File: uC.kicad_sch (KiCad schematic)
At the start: 11 parts, among them P12 Conn_02x10_Odd_Even, SW1 SW_MEC_5E, U2(J1) RPi-Pico

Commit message: Avances en corrección de errores en conexiones eléctricas (ERC).
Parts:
- gave numbers to parts that had none: 1
- renumbered C2 to C1, C1 to C2, D1 to D17, R19 to R1, R19 to R2, U2(J1) to U1
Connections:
- no-connect marks 8 -> 14

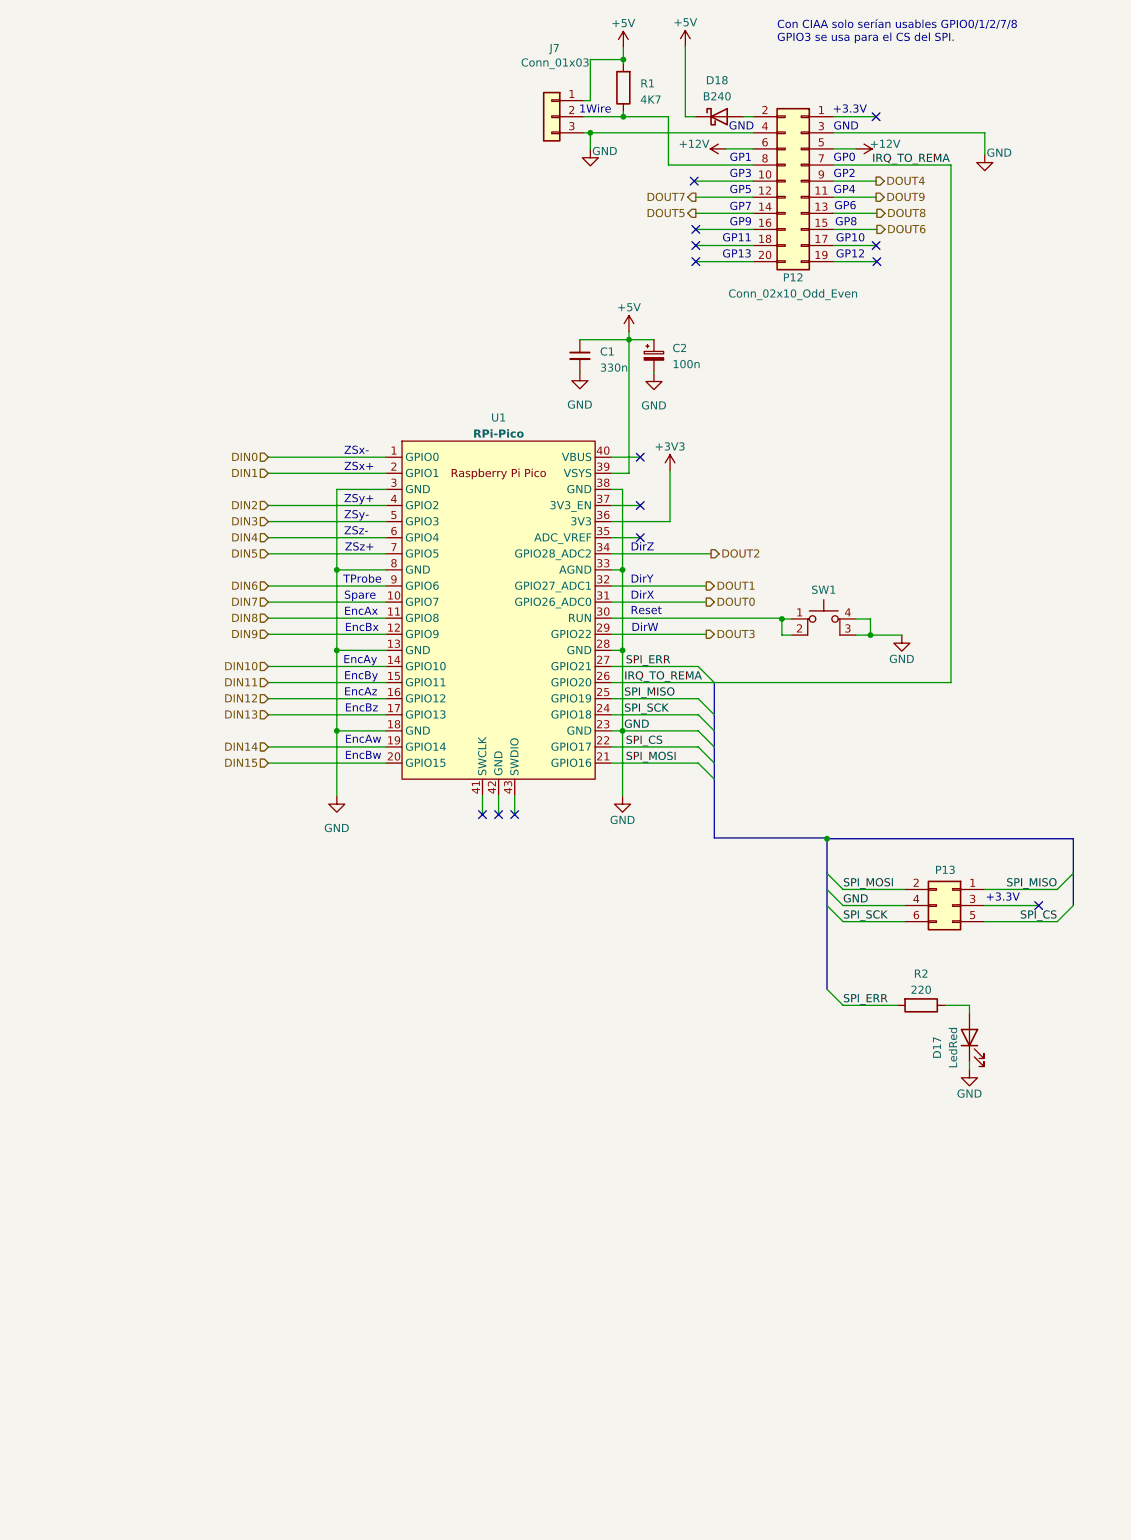
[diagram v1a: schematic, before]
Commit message: Se corrigieron errores de conexión. Falta asignar footprints aún
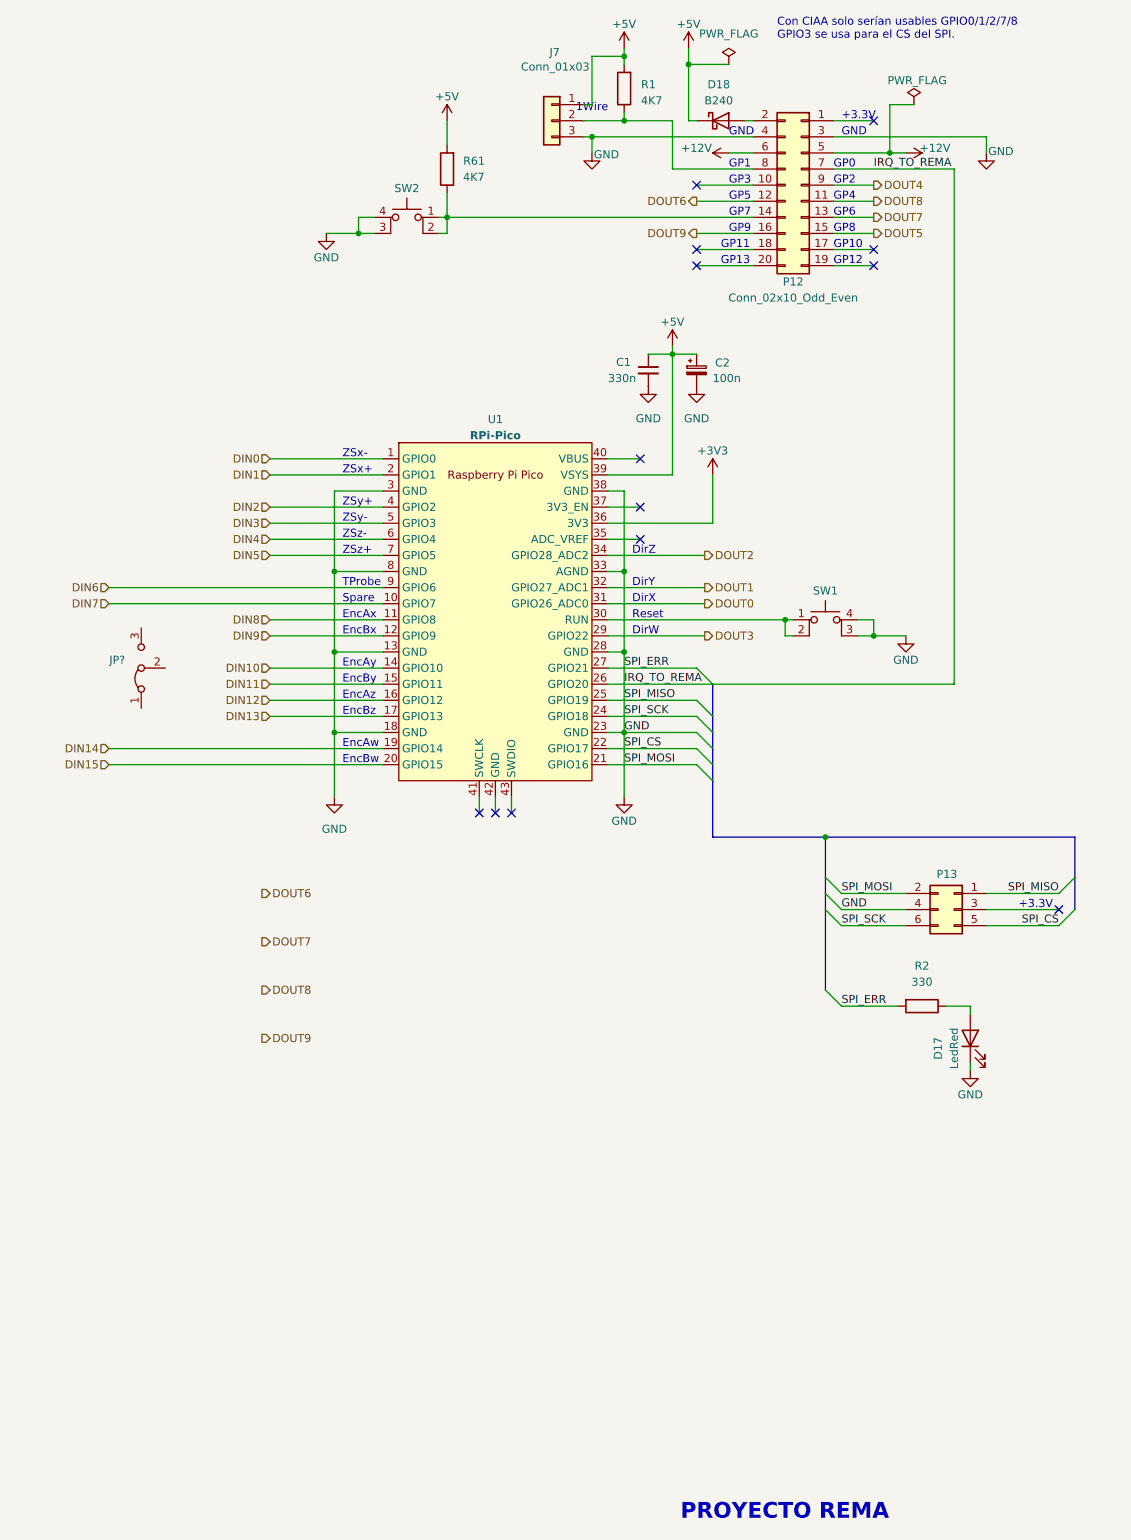
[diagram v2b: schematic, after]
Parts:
- added JP?: Jumper_3_Bridged12, symbol Jumper:Jumper_3_Bridged12
- added R61: 4K7, symbol Device:R
- added SW2: SW_MEC_5E, symbol Switch:SW_MEC_5E
- D17: footprint (none) -> LED_SMD:LED_1206_3216Metric
- R2: value 220 -> 330
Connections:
- net IRQ_TO_REMA is gone; now on net GND: P12.7 (Pin_7), U1.26 (GPIO20)
- net SPI_CS is gone; now on net GND: P13.5 (Pin_5), U1.22 (GPIO17)
- net SPI_ERR is gone; now on net GND: R2.2, U1.27 (GPIO21)
- net SPI_MISO is gone; now on net GND: P13.1 (Pin_1), U1.25 (GPIO19)
- net SPI_MOSI is gone; now on net GND: P13.2 (Pin_2), U1.21 (GPIO16)
- net SPI_SCK is gone; now on net GND: P13.6 (Pin_6), U1.24 (GPIO18)
- net +5V: now also R61.2
- net DOUT5: now also P12.15 (Pin_15); no longer P12.14 (Pin_14)
- net DOUT6: now also P12.12 (Pin_12); no longer P12.15 (Pin_15)
- net DOUT7: now also P12.13 (Pin_13); no longer P12.12 (Pin_12)
- net DOUT8: now also P12.11 (Pin_11); no longer P12.13 (Pin_13)
- net DOUT9: now also P12.16 (Pin_16); no longer P12.11 (Pin_11)
- net GND: now also SW2.3 (K), SW2.4 (A)
- new net: P12.14 (Pin_14), R61.1, SW2.1, SW2.2
- no-connect marks 14 -> 13
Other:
- note added: "PROYECTO REMA"
- title: (none) -> Microcontrolador y fuentes
- moved on the sheet: C1, C2, D18, J7, P12, P13, U1

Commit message: se agregan jumpers para elegir entre entradas/salidas
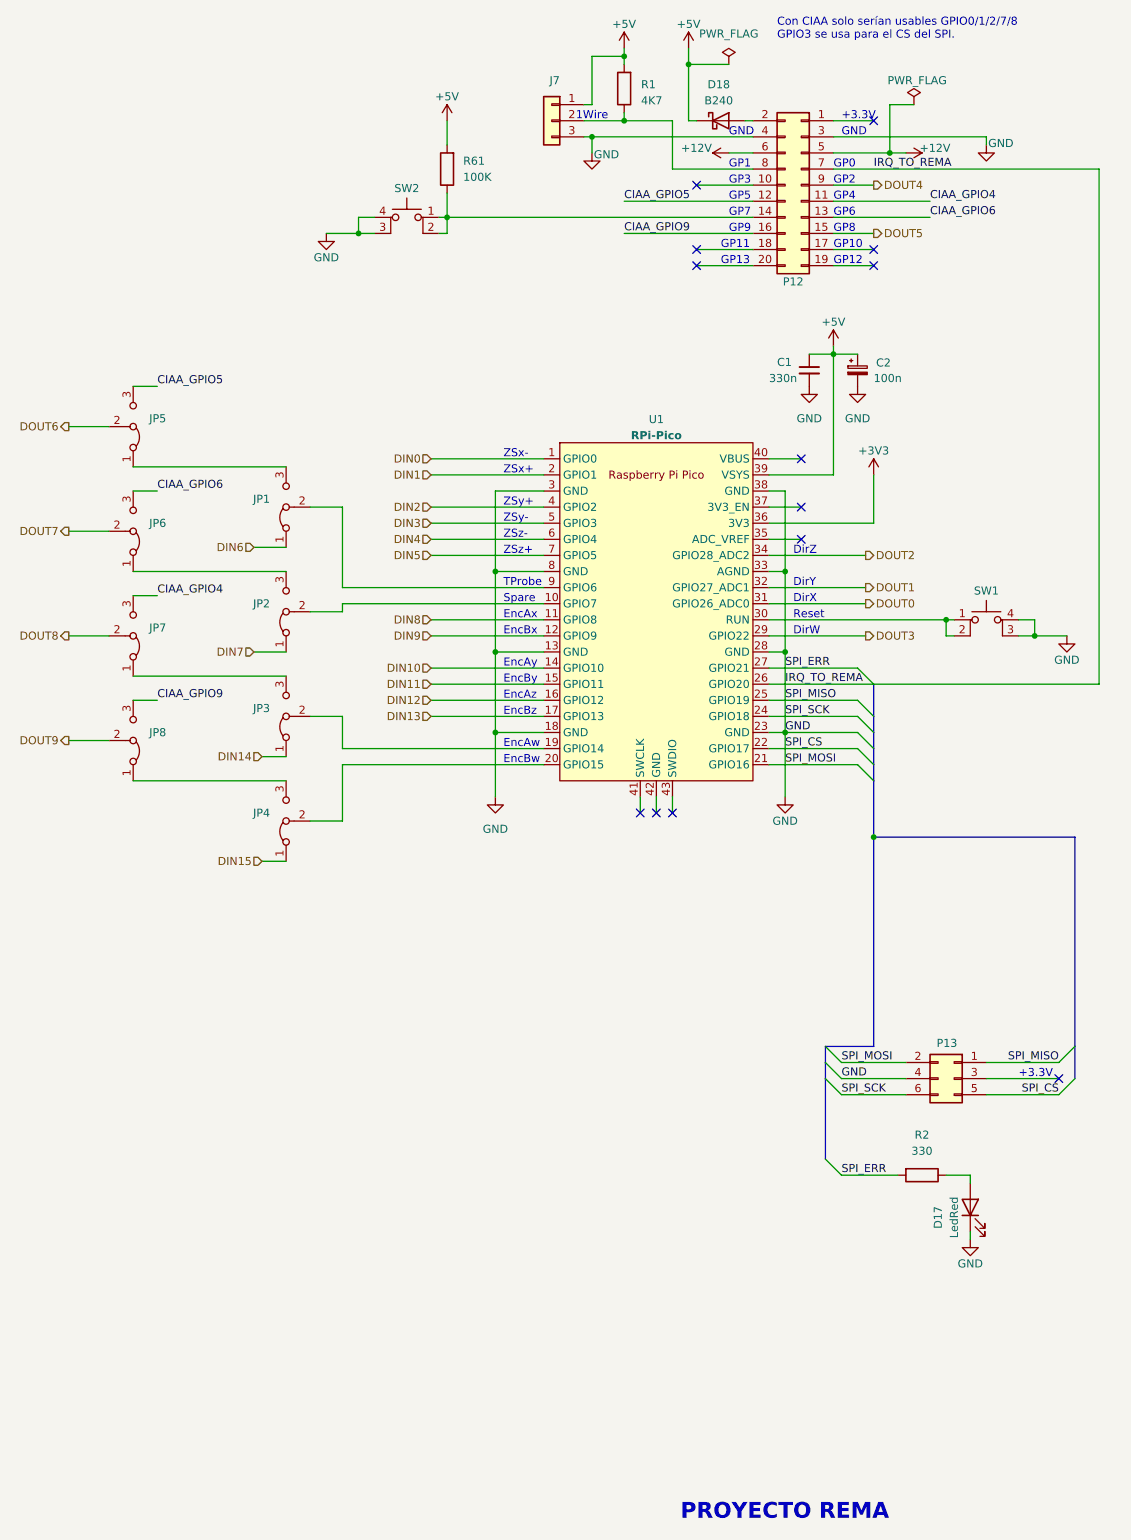
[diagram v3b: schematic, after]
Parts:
- added JP2, JP3, JP4, JP5, JP6, JP7, JP8: Jumper_3_Bridged12, Connector_PinHeader_1.00mm:PinHeader_1x03_P1.00mm_Vertical_SMD_Pin1Left, symbol Jumper:Jumper_3_Bridged12
- JP1: renamed from JP?; footprint (none) -> Connector_PinHeader_1.00mm:PinHeader_1x03_P1.00mm_Vertical_SMD_Pin1Left
- R61: value 4K7 -> 100K
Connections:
- net DIN14: now also JP3.1 (A); no longer U1.19 (GPIO14)
- net DIN15: now also JP4.1 (A); no longer U1.20 (GPIO15)
- net DIN6: now also JP1.1 (A); no longer U1.9 (GPIO6)
- net DIN7: now also JP2.1 (A); no longer U1.10 (GPIO7)
- net DOUT6: now also JP5.2 (C); no longer P12.12 (Pin_12)
- net DOUT7: now also JP6.2 (C); no longer P12.13 (Pin_13)
- net DOUT8: now also JP7.2 (C); no longer P12.11 (Pin_11)
- net DOUT9: now also JP8.2 (C); no longer P12.16 (Pin_16)
- net at JP1.2 (C): now also U1.9 (GPIO6)
- net at JP1.3 (B): now also JP5.1 (A)
- new net: JP2.3 (B), JP6.1 (A)
- new net: JP3.3 (B), JP7.1 (A)
- new net: JP2.2 (C), U1.10 (GPIO7)
- new net: JP3.2 (C), U1.19 (GPIO14)
- new net: JP4.2 (C), U1.20 (GPIO15)
- new net: JP4.3 (B), JP8.1 (A)
- new net CIAA_GPIO4: JP7.3 (B), P12.11 (Pin_11)
- new net CIAA_GPIO5: JP5.3 (B), P12.12 (Pin_12)
- new net CIAA_GPIO6: JP6.3 (B), P12.13 (Pin_13)
- new net CIAA_GPIO9: JP8.3 (B), P12.16 (Pin_16)
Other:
- moved on the sheet: C1, C2, D17, JP1, P13, R2, SW1, U1

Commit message: Esquemático listo, sin errores de conexión y con todos los footprints especificados
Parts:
- C1, C2: footprint (none) -> Capacitor_SMD:C_1206_3216Metric
- J7: footprint (none) -> Connector_PinHeader_2.54mm:PinHeader_1x05_P2.54mm_Vertical
- P12: footprint (none) -> Connector_PinHeader_2.54mm:PinHeader_2x10_P2.54mm_Vertical
- P13: footprint (none) -> Connector_PinHeader_2.54mm:PinHeader_2x03_P2.54mm_Vertical
- R1, R2, R61: footprint (none) -> Resistor_SMD:R_1206_3216Metric
- SW1, SW2: footprint (none) -> Button_Switch_SMD:SW_Push_1P1T_NO_CK_KSC7xxJ
- U1: footprint RPi_Pico:RPi_Pico_SMD_TH -> MCU_RaspberryPi_and_Boards:RPi_Pico_SMD_TH
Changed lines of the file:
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@@
 			)
 		)
-		(property "Footprint" "RPi_Pico:RPi_Pico_SMD_TH"
+		(property "Footprint" "MCU_RaspberryPi_and_Boards:RPi_Pico_SMD_TH"
 			(at 120.65 119.38 90)
 			(effects
@@
 			)
 		)
-		(property "Footprint" ""
+		(property "Footprint" "Button_Switch_SMD:SW_Push_1P1T_NO_CK_KSC7xxJ"
 			(at 81.28 52.07 0)
 			(effects
@@
 			)
 		)
-		(property "Footprint" ""
+		(property "Footprint" "Capacitor_SMD:C_1206_3216Metric"
 			(at 152.4 81.28 0)
 			(effects
@@
 			)
 		)
-		(property "Footprint" ""
+		(property "Footprint" "Resistor_SMD:R_1206_3216Metric"
 			(at 162.56 206.502 90)
 			(effects
@@
 			)
 		)
-		(property "Footprint" ""
+		(property "Footprint" "Button_Switch_SMD:SW_Push_1P1T_NO_CK_KSC7xxJ"
 			(at 172.72 115.57 0)
 			(effects
@@
 			)
 		)
-		(property "Footprint" ""
+		(property "Footprint" "Connector_PinHeader_2.54mm:PinHeader_2x10_P2.54mm_Vertical"
 			(at 143.51 52.07 0)
 			(effects
@@
 			)
 		)
-		(property "Footprint" ""
+		(property "Footprint" "Connector_PinHeader_2.54mm:PinHeader_1x05_P2.54mm_Vertical"
 			(at 104.14 41.91 0)
 			(effects
@@
 			)
 		)
-		(property "Footprint" ""
+		(property "Footprint" "Resistor_SMD:R_1206_3216Metric"
 			(at 89.408 49.53 90)
 			(effects
@@
 			)
 		)
-		(property "Footprint" ""
+		(property "Footprint" "Connector_PinHeader_2.54mm:PinHeader_2x03_P2.54mm_Vertical"
 			(at 167.64 193.04 0)
 			(effects
@@
 			)
 		)
-		(property "Footprint" ""
+		(property "Footprint" "Capacitor_SMD:C_1206_3216Metric"
 			(at 144.78 81.28 0)
 			(effects
@@
 			)
 		)
-		(property "Footprint" ""
+		(property "Footprint" "Resistor_SMD:R_1206_3216Metric"
 			(at 117.348 36.83 90)
 			(effects

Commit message: Comienza el diseño del pcb
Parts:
- removed R61: 100K, Resistor_SMD:R_1206_3216Metric, symbol Device:R
- removed SW1, SW2: SW_MEC_5E, Button_Switch_SMD:SW_Push_1P1T_NO_CK_KSC7xxJ, symbol Switch:SW_MEC_5E
- added SW1, SW2: SW_Push, Button_Switch_SMD:SW_Push_1P1T_NO_CK_KSC7xxJ, symbol Switch:SW_Push
- J7: footprint Connector_PinHeader_2.54mm:PinHeader_1x05_P2.54mm_Vertical -> Connector_PinHeader_2.54mm:PinHeader_1x03_P2.54mm_Vertical
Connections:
- net GND: now also SW1.2, SW2.1; no longer P12.7 (Pin_7), P13.1 (Pin_1), P13.2 (Pin_2), P13.5 (Pin_5), P13.6 (Pin_6), R2.2, U1.21 (GPIO16), U1.22 (GPIO17), U1.24 (GPIO18), U1.25 (GPIO19), U1.26 (GPIO20), U1.27 (GPIO21)
- net at U1.30 (RUN): now also SW1.1
- net at P12.14 (Pin_14): now also SW2.2
- new net IRQ_TO_REMA: P12.7 (Pin_7), U1.26 (GPIO20)
- new net SPI_CS: P13.5 (Pin_5), U1.22 (GPIO17)
- new net SPI_ERR: R2.2, U1.27 (GPIO21)
- new net SPI_MISO: P13.1 (Pin_1), U1.25 (GPIO19)
- new net SPI_MOSI: P13.2 (Pin_2), U1.21 (GPIO16)
- new net SPI_SCK: P13.6 (Pin_6), U1.24 (GPIO18)

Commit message: Se agregan divisores resisitivos a la salida de los schmitt triggers para asegurar que no le lleguen 5V a las entradas de la pico. Se acutaliza el pcb y se acomodan los componentes en dos capas
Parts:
- added TP3: TestPoint, TestPoint:TestPoint_Pad_D2.0mm, symbol Connector:TestPoint
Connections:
- net +3V3: now also TP3.1
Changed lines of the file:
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@@
 	)
 	(junction
+		(at 166.37 105.41)
+		(diameter 0)
+		(color 0 0 0 0)
+	)
+	(junction
 		(at 110.49 44.45)
 		(diameter 0)
@@
 	)
 	(junction
+		(at 154.94 105.41)
+		(diameter 0)
+		(color 0 0 0 0)
+	)
+	(junction
 		(at 95.25 125.73)
 		(diameter 0)
@@
 	(wire
 		(pts
+			(xy 166.37 99.06) (xy 166.37 105.41)
+		)
+		(stroke
+			(width 0)
+			(type default)
+		)
+	)
+	(wire
+		(pts
 			(xy 95.25 100.33) (xy 95.25 113.03)
 		)
@@
 	(wire
 		(pts
+			(xy 173.99 105.41) (xy 166.37 105.41)
+		)
+		(stroke
+			(width 0)
+			(type default)
+		)
+	)
+	(wire
+		(pts
 			(xy 180.34 120.65) (xy 180.34 123.19)
 		)
@@
 	(wire
 		(pts
+			(xy 173.99 104.14) (xy 173.99 105.41)
+		)
+		(stroke
+			(width 0)
+			(type default)
+		)
+	)
+	(wire
+		(pts
 			(xy 127 52.07) (xy 135.89 52.07)
 		)
@@
 	(wire
 		(pts
+			(xy 166.37 105.41) (xy 154.94 105.41)
+		)
+		(stroke
+			(width 0)
+			(type default)
+		)
+	)
+	(wire
+		(pts
 			(xy 110.49 44.45) (xy 110.49 46.99)
 		)
@@
 	)
 	(symbol
+		(lib_id "Connector:TestPoint")
+		(at 166.37 99.06 0)
+		(unit 1)
+		(exclude_from_sim yes)
+		(in_bom yes)
+		(on_board yes)
+		(dnp no)
+		(property "Reference" "TP3"
+			(at 162.56 93.98 0)
+			(effects
+				(font
+					(size 1.27 1.27)
+				)
+				(justify left)
+			)
+		)
+		(property "Value" "TestPoint"
+			(at 156.21 97.79 0)
+			(effects
+				(font
+					(size 1.27 1.27)
+				)
+				(justify left)
+				(hide yes)
+			)
+		)
+		(property "Footprint" "TestPoint:TestPoint_Pad_D2.0mm"
+			(at 171.45 99.06 0)
+			(effects
+				(font
+					(size 1.27 1.27)
+				)
+				(hide yes)
+			)
+		)
+		(property "Datasheet" "~"
+			(at 171.45 99.06 0)
+			(effects
+				(font
+					(size 1.27 1.27)
+				)
+				(hide yes)
+			)
+		)
+		(property "Description" "test point"
+			(at 166.37 99.06 0)
+			(effects
+				(font
+					(size 1.27 1.27)
+				)
+				(hide yes)
+			)
+		)
+		(pin "1"
+		)
+		(instances
+			(project "PonchoRema"
+				(path "/5eaa4ad0-b04c-4c59-839d-734ec887be48/2878f7e1-5ffb-47b6-a169-135caa320801"
+					(reference "TP3")
+					(unit 1)
+				)
+			)
+		)
+	)
+	(symbol
 		(lib_id "power:+5V")
 		(at 148.59 77.47 0)
@@
 		(at 95.25 57.15 0)
 		(unit 1)
-		(exclude_from_sim no)
+		(exclude_from_sim yes)
 		(in_bom yes)
 		(on_board yes)
@@
 	)
 	(symbol
+		(lib_id "power:PWR_FLAG")
+		(at 173.99 104.14 0)
+		(unit 1)
+		(exclude_from_sim no)
+		(in_bom yes)
+		(on_board yes)
+		(dnp no)
+		(fields_autoplaced yes)
+		(property "Reference" "#FLG02"
+			(at 173.99 102.235 0)
+			(effects
+				(font
+					(size 1.27 1.27)
+				)
+				(hide yes)
+			)
+		)
+		(property "Value" "PWR_FLAG"
+			(at 173.99 99.314 0)
+			(effects
+				(font
+					(size 1.27 1.27)
+				)
+			)
+		)
+		(property "Footprint" ""
+			(at 173.99 104.14 0)
+			(effects
+				(font
+					(size 1.27 1.27)
+				)
+				(hide yes)
+			)
+		)
+		(property "Datasheet" "~"
+			(at 173.99 104.14 0)
+			(effects
+				(font
+					(size 1.27 1.27)
+				)
+				(hide yes)
+			)
+		)
+		(property "Description" "Special symbol for telling ERC where power comes from"
+			(at 173.99 104.14 0)
+			(effects
+				(font
+					(size 1.27 1.27)
+				)
+				(hide yes)
+			)
+		)
+		(pin "1"
+		)
+		(instances
+			(project "PonchoRema"
+				(path "/5eaa4ad0-b04c-4c59-839d-734ec887be48/2878f7e1-5ffb-47b6-a169-135caa320801"
+					(reference "#FLG02")
+					(unit 1)
+				)
+			)
+		)
+	)
+	(symbol
 		(lib_id "power:GND")
 		(at 180.34 123.19 0)
@@
 		(at 172.72 120.65 0)
 		(unit 1)
-		(exclude_from_sim no)
+		(exclude_from_sim yes)
 		(in_bom yes)
 		(on_board yes)
